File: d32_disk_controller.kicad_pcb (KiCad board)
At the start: 4 copper layers, 107.5 x 74.2 mm, 21 parts, among them J1 Clock_Test, J2 IDC_Floppy, J3 EDGE, J4 JTAG, U1 27C64, U10 ATF1504AS-xAx44, U2 WD2797, U6 74HCT04, Y1 4MHz

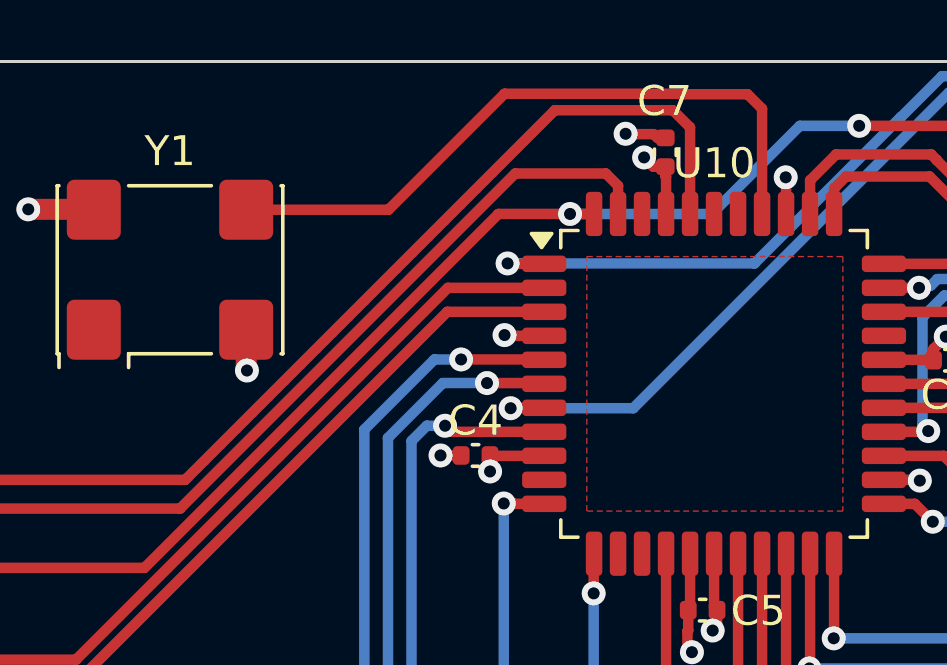
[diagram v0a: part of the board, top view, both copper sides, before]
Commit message: add CPLD bin files
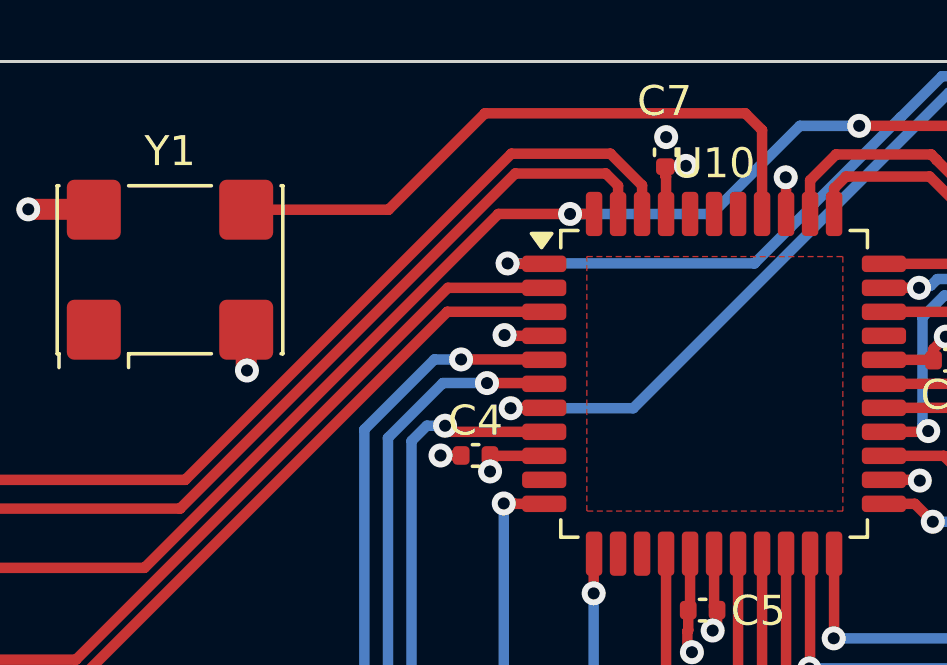
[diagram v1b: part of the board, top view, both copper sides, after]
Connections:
- U10 pad 40: ~{NMI} -> unconnected-(U10-I/OE2/GCLK2-Pad40)
- U10 pad 42: unconnected-(U10-I/O-Pad42) -> ~{NMI}
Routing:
- net ~{NMI}: track 45.8 -> 41.9 mm
- net GND: track 32.5 -> 31.0 mm
- net /raw_clock: track 23.0 -> 22.1 mm
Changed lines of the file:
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@@
 	(net 77 "unconnected-(U2-HLT-Pad40)")
 	(net 78 "unconnected-(U10-I{slash}O-Pad30)")
-	(net 79 "unconnected-(U10-I{slash}O-Pad42)")
+	(net 79 "unconnected-(U10-I{slash}OE2{slash}GCLK2-Pad40)")
 	(net 80 "unconnected-(C3-Pad3)")
 	(net 81 "unconnected-(Y1-EN-Pad1)")
@@
 			(layers "F.Cu" "F.Mask" "F.Paste")
 			(roundrect_rratio 0.25)
-			(net 26 "~{NMI}")
+			(net 79 "unconnected-(U10-I{slash}OE2{slash}GCLK2-Pad40)")
 			(pinfunction "I/OE2/GCLK2")
-			(pintype "input")
+			(pintype "input+no_connect")
 		)
 		(pad "41" smd roundrect
@@
 			(layers "F.Cu" "F.Mask" "F.Paste")
 			(roundrect_rratio 0.25)
-			(net 79 "unconnected-(U10-I{slash}O-Pad42)")
+			(net 26 "~{NMI}")
 			(pinfunction "I/O")
-			(pintype "bidirectional+no_connect")
+			(pintype "bidirectional")
 		)
 		(pad "43" smd roundrect
@@
 	)
 	(segment
-		(start 89.372758 24.8464)
-		(end 89.33775 24.8464)
-		(width 0.35)
-		(layer "F.Cu")
-		(net 1)
-	)
-	(segment
 		(start 54.254 75.4759)
 		(end 62.3312 75.4759)
@@
 	)
 	(segment
-		(start 89.33775 24.8464)
-		(end 89.20212 24.71077)
-		(width 0.35)
-		(layer "F.Cu")
-		(net 1)
-	)
-	(segment
 		(start 124.4088 54.5971)
 		(end 124.3834 54.6225)
@@
 	)
 	(segment
-		(start 90.263012 24.8464)
-		(end 90.139315 24.722703)
-		(width 0.35)
-		(layer "F.Cu")
-		(net 1)
-	)
-	(segment
 		(start 100.4264 32.258)
 		(end 101.0412 32.258)
@@
 	)
 	(segment
-		(start 89.496455 24.722703)
-		(end 89.372758 24.8464)
-		(width 0.35)
-		(layer "F.Cu")
-		(net 1)
-	)
-	(segment
-		(start 90.5256 24.8464)
-		(end 90.263012 24.8464)
+		(start 90.551033 24.820967)
+		(end 90.5256 24.8464)
 		(width 0.35)
 		(layer "F.Cu")
@@
 	)
 	(segment
-		(start 90.139315 24.722703)
-		(end 89.496455 24.722703)
-		(width 0.35)
-		(layer "F.Cu")
-		(net 1)
-	)
-	(segment
 		(start 98.9834 36.2454)
 		(end 99.0092 36.2712)
@@
 	)
 	(segment
+		(start 90.553194 24.820967)
+		(end 90.551033 24.820967)
+		(width 0.35)
+		(layer "F.Cu")
+		(net 1)
+	)
+	(segment
 		(start 91.3512 40.5282)
 		(end 91.2902 40.5892)
@@
 	)
 	(via
-		(at 89.20212 24.71077)
+		(at 90.553194 24.820967)
 		(size 0.8)
 		(drill 0.4)
@@
 	)
 	(segment
-		(start 90.7796 23.9268)
-		(end 86.8426 23.9268)
+		(start 85.3948 25.3746)
+		(end 74.5236 36.2458)
 		(width 0.35)
 		(layer "F.Cu")
@@
 	)
 	(segment
-		(start 86.8426 23.9268)
-		(end 74.5236 36.2458)
+		(start 74.5236 36.2458)
+		(end 63.0549 36.2458)
 		(width 0.35)
 		(layer "F.Cu")
@@
 	)
 	(segment
-		(start 74.5236 36.2458)
-		(end 63.0549 36.2458)
+		(start 89.7512 27.3829)
+		(end 89.7512 26.429)
 		(width 0.35)
 		(layer "F.Cu")
@@
 	)
 	(segment
-		(start 91.3512 24.4984)
-		(end 90.7796 23.9268)
+		(start 88.6968 25.3746)
+		(end 85.3948 25.3746)
 		(width 0.35)
 		(layer "F.Cu")
@@
 	)
 	(segment
-		(start 91.3512 27.3829)
-		(end 91.3512 24.4984)
+		(start 89.7512 26.429)
+		(end 88.6968 25.3746)
 		(width 0.35)
 		(layer "F.Cu")
@@
 	)
 	(segment
+		(start 90.551 25.781)
+		(end 90.5256 25.8064)
+		(width 0.35)
+		(layer "F.Cu")
+		(net 31)
+	)
+	(segment
 		(start 84.681 35.9638)
 		(end 84.6836 35.9664)
@@
 	)
 	(segment
-		(start 90.125582 25.8064)
-		(end 89.817885 25.498703)
-		(width 0.35)
-		(layer "F.Cu")
-		(net 31)
-	)
-	(segment
 		(start 84.681 35.433)
 		(end 84.681 35.9638)
@@
 	)
 	(segment
-		(start 90.5256 25.8064)
-		(end 90.125582 25.8064)
-		(width 0.35)
-		(layer "F.Cu")
-		(net 31)
-	)
-	(segment
 		(start 92.2502 41.123619)
 		(end 92.2502 40.5892)
@@
 	)
 	(segment
+		(start 91.2114 25.781)
+		(end 90.551 25.781)
+		(width 0.35)
+		(layer "F.Cu")
+		(net 31)
+	)
+	(segment
 		(start 99.4538 32.2454)
 		(end 97.8137 32.2454)
@@
 	)
 	(via
-		(at 89.817885 25.498703)
+		(at 91.2114 25.781)
 		(size 0.8)
 		(drill 0.4)
@@
 	)
 	(segment
-		(start 91.025432 23.3934)
-		(end 91.007832 23.3758)
+		(start 93.1926 24.0284)
+		(end 84.513968 24.0284)
 		(width 0.35)
 		(layer "F.Cu")
@@
 	)
 	(segment
-		(start 93.7512 27.3829)
-		(end 93.7512 23.8758)
+		(start 93.7512 24.587)
+		(end 93.1926 24.0284)
 		(width 0.35)
 		(layer "F.Cu")
@@
 	)
 	(segment
-		(start 93.7512 23.8758)
-		(end 93.2688 23.3934)
-		(width 0.35)
-		(layer "F.Cu")
-		(net 60)
-	)
-	(segment
-		(start 85.166568 23.3758)
-		(end 81.300368 27.242)
-		(width 0.35)
-		(layer "F.Cu")
-		(net 60)
-	)
-	(segment
-		(start 93.2688 23.3934)
-		(end 91.025432 23.3934)
+		(start 93.7512 27.3829)
+		(end 93.7512 24.587)
 		(width 0.35)
 		(layer "F.Cu")
@@
 	)
 	(segment
-		(start 91.007832 23.3758)
-		(end 85.166568 23.3758)
+		(start 84.513968 24.0284)
+		(end 81.300368 27.242)
 		(width 0.35)
 		(layer "F.Cu")
